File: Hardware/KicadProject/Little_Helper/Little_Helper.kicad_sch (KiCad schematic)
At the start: 1 part, among them U1 ESP32-S3-MINI-1

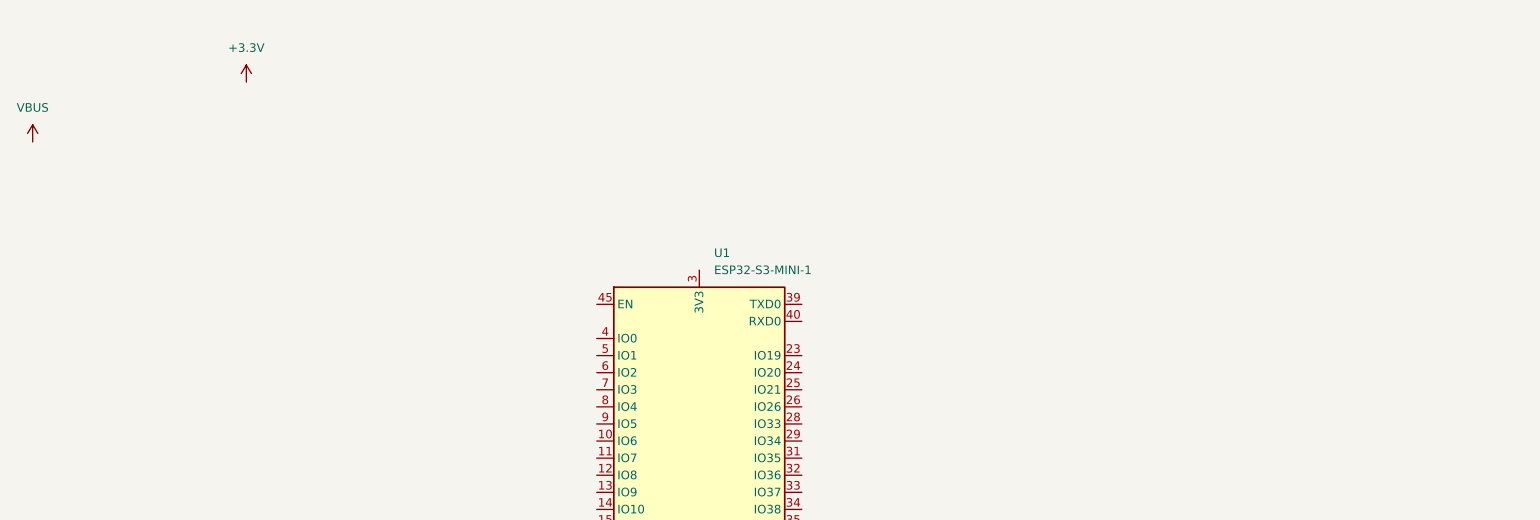
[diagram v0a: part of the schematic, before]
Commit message: fix some library mismatch
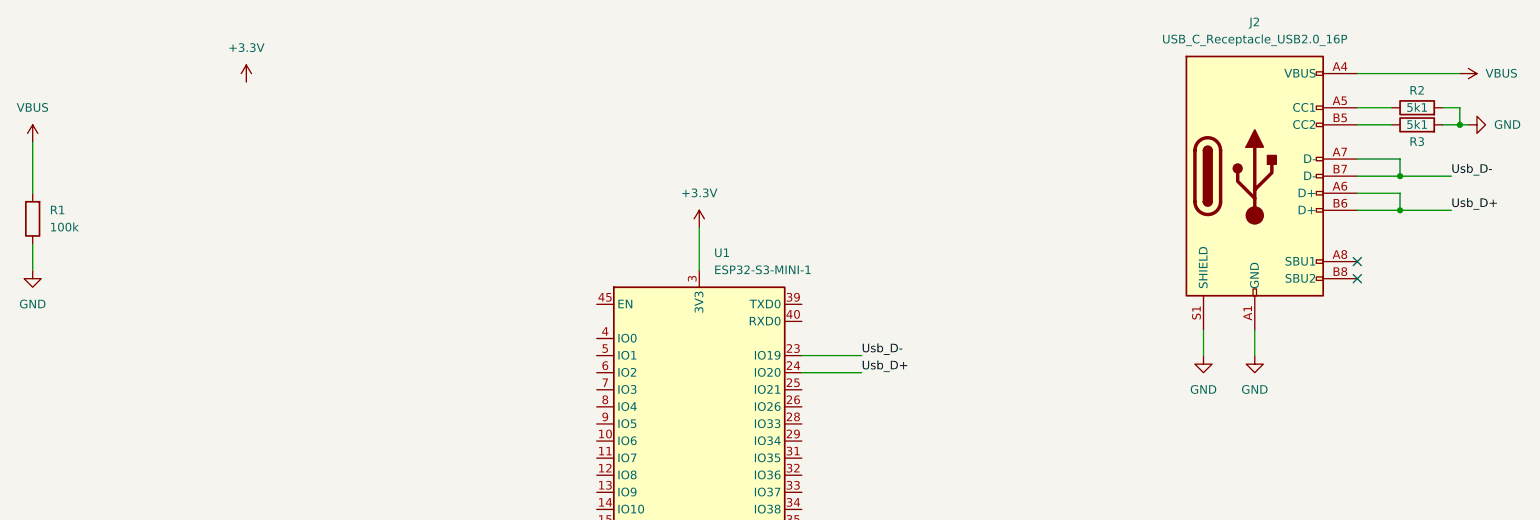
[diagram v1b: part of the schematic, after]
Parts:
- added J2: USB_C_Receptacle_USB2.0_16P, Connector_USB:USB_C_Receptacle_G-Switch_GT-USB-7010ASV, symbol Connector:USB_C_Receptacle_USB2.0_16P
- added R1: 100k, Resistor_SMD:R_0805_2012Metric, symbol Device:R
- added R2, R3: 5k1, Resistor_SMD:R_0805_2012Metric, symbol Device:R
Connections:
- net +3.3V: now also U1.3 (3V3)
- net GND: now also J2.A1 (GND), J2.A12 (GND), J2.B1 (GND), J2.B12 (GND), J2.S1 (SHIELD), R1.1, R2.2, R3.2
- net VBUS: now also J2.A4 (VBUS), J2.A9 (VBUS), J2.B4 (VBUS), J2.B9 (VBUS), R1.2
- net Usb_D-: now reaches U1.23 (IO19)
- net Usb_D-: now also J2.A7 (D-), J2.B7 (D-)
- net Usb_D+: now reaches U1.24 (IO20)
- net Usb_D+: now also J2.A6 (D+), J2.B6 (D+)
- new net: J2.A5 (CC1), R2.1
- new net: J2.B5 (CC2), R3.1
- no-connect marks 0 -> 2

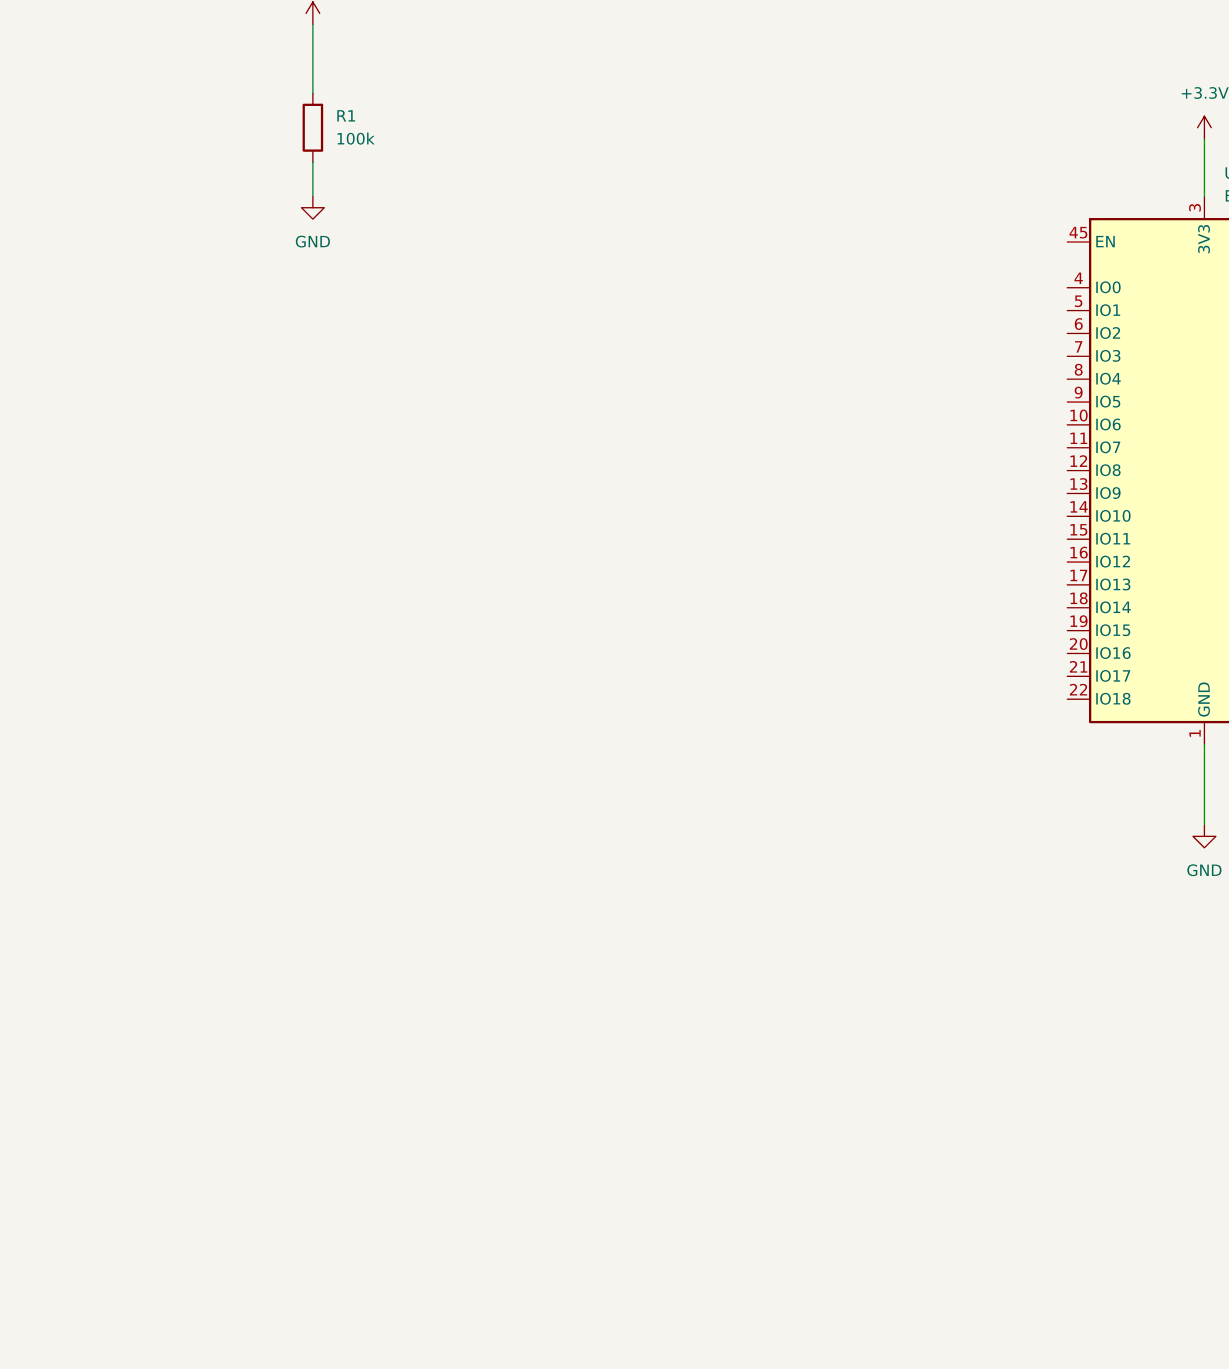
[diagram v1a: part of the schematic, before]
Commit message: add tactile buttons
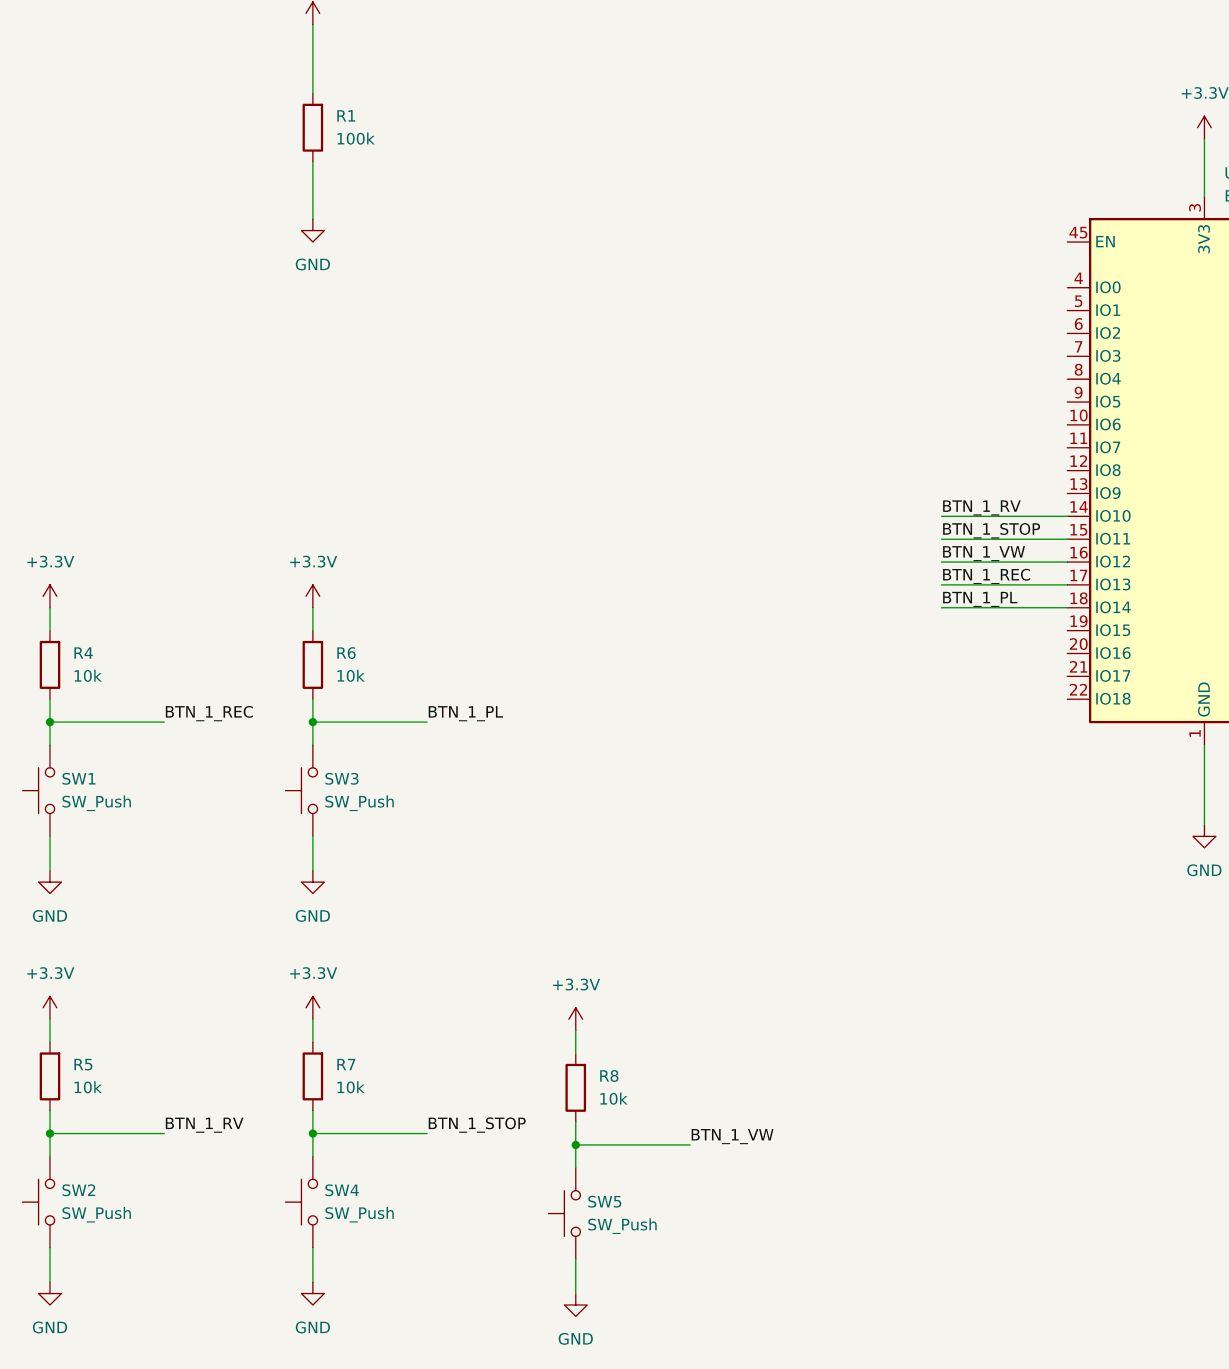
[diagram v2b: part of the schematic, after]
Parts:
- added R4, R5, R6, R7, R8: 10k, Resistor_SMD:R_0805_2012Metric, symbol Device:R
- added SW1, SW2, SW3, SW4, SW5: SW_Push, Button_Switch_THT:SW_PUSH_6mm_H5mm, symbol Switch:SW_Push
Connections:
- net +3.3V: now also R4.2, R5.2, R6.2, R7.2, R8.2
- net GND: now also SW1.1, SW2.1, SW3.1, SW4.1, SW5.1
- net BTN_1_RV: now reaches U1.14 (IO10)
- net BTN_1_RV: now also R5.1, SW2.2
- net BTN_1_STOP: now reaches U1.15 (IO11)
- net BTN_1_STOP: now also R7.1, SW4.2
- net BTN_1_VW: now reaches U1.16 (IO12)
- net BTN_1_VW: now also R8.1, SW5.2
- net BTN_1_REC: now reaches U1.17 (IO13)
- net BTN_1_REC: now also R4.1, SW1.2
- net BTN_1_PL: now reaches U1.18 (IO14)
- net BTN_1_PL: now also R6.1, SW3.2

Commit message: board in progress
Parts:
- removed J2: USB_C_Receptacle_USB2.0_16P, Connector_USB:USB_C_Receptacle_G-Switch_GT-USB-7010ASV, symbol Connector:USB_C_Receptacle_USB2.0_16P
- removed R2, R3: 5k1, Resistor_SMD:R_0805_2012Metric, symbol Device:R
- added C1, C2, C3, C4, C5, C6, C8: 10uF, Capacitor_SMD:C_0603_1608Metric, symbol PCM_Capacitor_AKL:C_0603
- added C7, C9: 1uF, Capacitor_SMD:C_0603_1608Metric, symbol PCM_Capacitor_AKL:C_0603
- added D1: MBR0540, Diode_SMD:D_0805_2012Metric, symbol PCM_Diode_Schottky_AKL:MBR0540
- added D2: LED, LED_SMD:LED_0603_1608Metric, symbol Device:LED
- added D3: WS2812B, LED_SMD:LED_WS2812B_PLCC4_5.0x5.0mm_P3.2mm, symbol LED:WS2812B
- added D4: BAS16, ba_sot:sot_23, symbol ba_diode:BAS16
- added J1: USB_B_Micro, Connector_USB:USB_Micro-B_Wuerth_629105150521_CircularHoles, symbol Connector:USB_B_Micro
- added J2: Conn_01x02_Pin, Connector_Hirose:Hirose_DF13-02P-1.25DSA_1x02_P1.25mm_Vertical, symbol Connector:Conn_01x02_Pin
- added Q1: DMG3415U, Package_TO_SOT_SMD:SOT-23, symbol PCM_Transistor_MOSFET_AKL:DMG3415U
- added R10, R11: 5k1, Resistor_SMD:R_0805_2012Metric, symbol Device:R
- added R3: R2012_100K, ba_res:r2012, symbol ba_res2012:R2012_100K
- added R9: 10k, Resistor_SMD:R_0805_2012Metric, symbol Device:R
- added SW6: SW_SPST, Button_Switch_SMD:SW_SPDT_CK_JS102011SAQN, symbol Switch:SW_SPST
- added SW7, SW8: SW_Push, Button_Switch_SMD:SW_Push_1P1T_NO_Vertical_Wuerth_434133025816, symbol Switch:SW_Push
- added U1: AP2112K-3.3, Package_TO_SOT_SMD:SOT-23-5, symbol Regulator_Linear:AP2112K-3.3
- added U3: MCP73831-2-OT, Package_TO_SOT_SMD:SOT-23-5, symbol Battery_Management:MCP73831-2-OT
- R1: value 100k -> 5k1
- R4: value 10k -> 100k
- renumbered U1 to U2
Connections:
- net +3.3V: now also R1.1, C1.1, C2.1, C3.1, C5.1, C6.1, C7.1, D4.1 (A), R9.2, U1.5 (VOUT); no longer R4.2
- net BTN_1_PL: now also SW5.2, R9.1; no longer R6.1, SW3.2
- net BTN_1_REC: now also R8.1, SW4.2; no longer R4.1, SW1.2
- net BTN_1_RV: now also SW1.2; no longer SW2.2
- net BTN_1_STOP: now also R6.1, SW2.2; no longer R7.1, SW4.2
- net BTN_1_VW: now also R7.1, SW3.2; no longer R8.1, SW5.2
- net GND: now also C1.2, C2.2, C3.2, C4.2, C5.2, C6.2, C7.2, C8.2, C9.2, D3.3 (VSS), J1.4 (ID), J1.5 (GND), J1.6 (Shield), J2.1 (Pin_1), R11.1, R3.2, SW7.1, SW8.1, U1.2 (GND), U3.2 (V_{SS}); no longer R1.1
- net Usb_D+: now also J1.3 (D+)
- net Usb_D-: now also J1.2 (D-)
- net VBUS: now also D1.2 (A), J1.1 (VBUS), Q1.1 (G), R10.1, R3.1, U3.4 (V_{DD}); no longer R1.2
- net NEOPIX: now reaches U2.28 (IO33)
- net NEOPIX: now also D3.4 (DIN)
- net BOOT0: now reaches U2.4 (IO0)
- net BOOT0: now also SW8.2
- net RESET: now reaches U2.45 (EN)
- net RESET: now also R1.2, C9.1, SW7.2
- new net: J2.2 (Pin_2), SW6.2 (B)
- new net: D2.1 (K), U3.1 (STAT)
- new net: D2.2 (A), R10.2
- new net: R11.2, U3.5 (PROG)
- new net: R4.1, U1.3 (EN)
- new net +BATT: C8.1, Q1.3 (D), SW6.1 (A), U3.3 (V_{BAT})
- new net NEOPIX_VDD: C4.1, D1.1 (K), D3.1 (VDD), D4.3 (K), Q1.2 (S), R4.2, U1.1 (VIN)
- no-connect marks 2 -> 32
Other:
- note added: "Orange"
- title: (none) -> Little_Helper
- moved on the sheet: U2

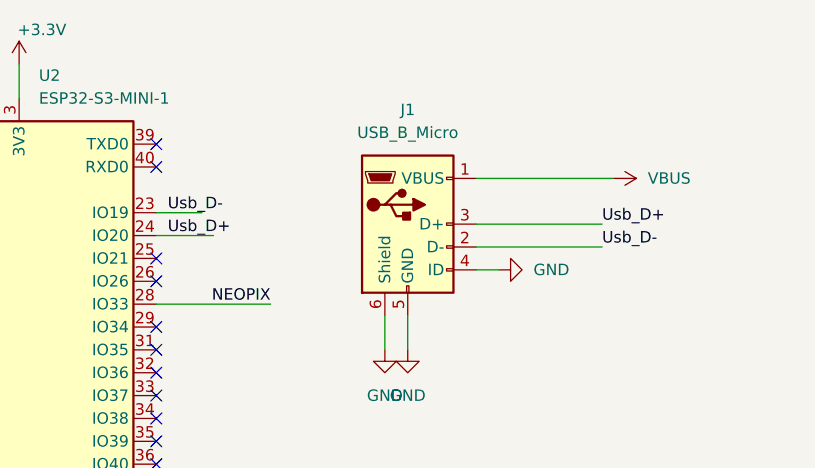
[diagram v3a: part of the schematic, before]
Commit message: change usb micro connector
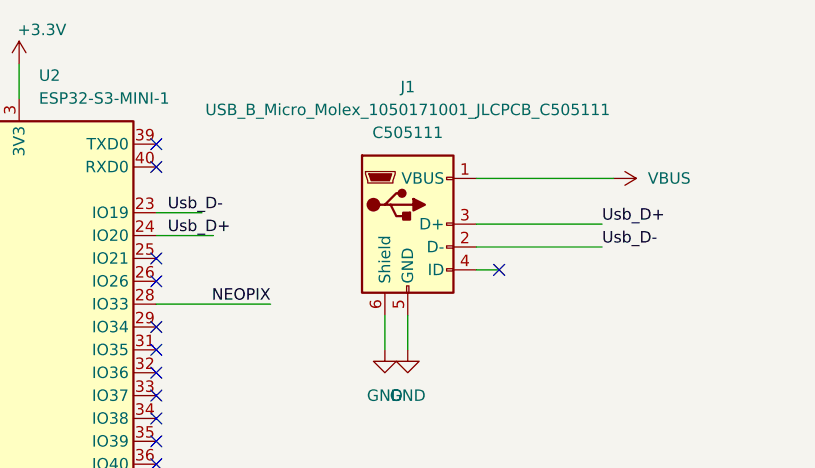
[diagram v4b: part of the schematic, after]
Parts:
- removed J1: USB_B_Micro, Connector_USB:USB_Micro-B_Wuerth_629105150521_CircularHoles, symbol Connector:USB_B_Micro
- added J1: USB_B_Micro_Molex_1050171001_JLCPCB_C505111, Connector_USB:USB_Micro-B_Molex-105017-0001, symbol Connector_USB_WOLKE:USB_B_Micro_Molex_1050171001_JLCPCB_C505111
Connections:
- net GND: now also J1.5 (GND), J1.6 (Shield)
- net Usb_D+: now also J1.3 (D+)
- net Usb_D-: now also J1.2 (D-)
- net VBUS: now also J1.1 (VBUS)
- no-connect marks 32 -> 33
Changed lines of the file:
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@@
 	)
 	(no_connect
+		(at 250.19 40.64)
+	)
+	(no_connect
 		(at 212.09 54.61)
 	)
@@
 	)
 	(symbol
+		(lib_id "Connector_USB_WOLKE:USB_B_Micro_Molex_1050171001_JLCPCB_C505111")
+		(at 240.03 35.56 0)
+		(unit 1)
+		(exclude_from_sim no)
+		(in_bom yes)
+		(on_board yes)
+		(dnp no)
+		(fields_autoplaced yes)
+		(property "Reference" "J1"
+			(at 240.03 20.32 0)
+			(effects
+				(font
+					(size 1.27 1.27)
+				)
+			)
+		)
+		(property "Value" "USB_B_Micro_Molex_1050171001_JLCPCB_C505111"
+			(at 240.03 22.86 0)
+			(effects
+				(font
+					(size 1.27 1.27)
+				)
+			)
+		)
+		(property "Footprint" "Connector_USB:USB_Micro-B_Molex-105017-0001"
+			(at 243.84 36.83 0)
+			(effects
+				(font
+					(size 1.27 1.27)
+				)
+				(hide yes)
+			)
+		)
+		(property "Datasheet" "https://wmsc.lcsc.com/wmsc/upload/file/pdf/v2/lcsc/2004301811_MOLEX-1050171001_C505111.pdf"
+			(at 243.84 36.83 0)
+			(effects
+				(font
+					(size 1.27 1.27)
+				)
+				(hide yes)
+			)
+		)
+		(property "Description" "USB Micro Type B connector"
+			(at 240.03 35.56 0)
+			(effects
+				(font
+					(size 1.27 1.27)
+				)
+				(hide yes)
+			)
+		)
+		(property "MPN" "1050171001"
+			(at 240.03 35.56 0)
+			(effects
+				(font
+					(size 1.27 1.27)
+				)
+				(hide yes)
+			)
+		)
+		(property "MN" "Molex"
+			(at 240.03 35.56 0)
+			(effects
+				(font
+					(size 1.27 1.27)
+				)
+				(hide yes)
+			)
+		)
+		(property "S3N" "JLCPCB"
+			(at 240.03 35.56 0)
+			(effects
+				(font
+					(size 1.27 1.27)
+				)
+				(hide yes)
+			)
+		)
+		(property "S3PN" "C505111"
+			(at 240.03 35.56 0)
+			(effects
+				(font
+					(size 1.27 1.27)
+				)
+				(hide yes)
+			)
+		)
+		(property "LCSC Part #" "C505111"
+			(at 240.03 25.4 0)
+			(effects
+				(font
+					(size 1.27 1.27)
+				)
+			)
+		)
+		(pin "1"
+		)
+		(pin "3"
+		)
+		(pin "5"
+		)
+		(pin "2"
+		)
+		(pin "6"
+		)
+		(pin "4"
+		)
+		(instances
+			(project ""
+				(path "/be456eed-bb99-4947-8d6f-815aa9683d71"
+					(reference "J1")
+					(unit 1)
+				)
+			)
+		)
+	)
+	(symbol
 		(lib_id "Device:LED")
 		(at 134.62 40.64 0)
@@
 	)
 	(symbol
-		(lib_id "Connector:USB_B_Micro")
-		(at 240.03 35.56 0)
-		(unit 1)
-		(exclude_from_sim no)
-		(in_bom yes)
-		(on_board yes)
-		(dnp no)
-		(fields_autoplaced yes)
-		(property "Reference" "J1"
-			(at 240.03 22.86 0)
-			(effects
-				(font
-					(size 1.27 1.27)
-				)
-			)
-		)
-		(property "Value" "USB_B_Micro"
-			(at 240.03 25.4 0)
-			(effects
-				(font
-					(size 1.27 1.27)
-				)
-			)
-		)
-		(property "Footprint" "Connector_USB:USB_Micro-B_Wuerth_629105150521_CircularHoles"
-			(at 243.84 36.83 0)
-			(effects
-				(font
-					(size 1.27 1.27)
-				)
-				(hide yes)
-			)
-		)
-		(property "Datasheet" "~"
-			(at 243.84 36.83 0)
-			(effects
-				(font
-					(size 1.27 1.27)
-				)
-				(hide yes)
-			)
-		)
-		(property "Description" "USB Micro Type B connector"
-			(at 240.03 35.56 0)
-			(effects
-				(font
-					(size 1.27 1.27)
-				)
-				(hide yes)
-			)
-		)
-		(pin "6"
-		)
-		(pin "2"
-		)
-		(pin "1"
-		)
-		(pin "4"
-		)
-		(pin "3"
-		)
-		(pin "5"
-		)
-		(instances
-			(project "Little_Helper"
-				(path "/be456eed-bb99-4947-8d6f-815aa9683d71"
-					(reference "J1")
-					(unit 1)
-				)
-			)
-		)
-	)
-	(symbol
 		(lib_id "power:+BATT")
 		(at 59.69 88.9 0)
@@
 					(unit 1)
 				)
-			)
-		)
-	)
-	(symbol
-		(lib_id "power:GND")
-		(at 250.19 40.64 90)
-		(unit 1)
-		(exclude_from_sim no)
-		(in_bom yes)
-		(on_board yes)
-		(dnp no)
-		(fields_autoplaced yes)
-		(property "Reference" "#PWR08"
-			(at 256.54 40.64 0)
-			(effects
-				(font
-					(size 1.27 1.27)
-				)
-				(hide yes)
-			)
-		)
-		(property "Value" "GND"
-			(at 254 40.6399 90)
-			(effects
-				(font
-					(size 1.27 1.27)
-				)
-				(justify right)
-			)
-		)
-		(property "Footprint" ""
-			(at 250.19 40.64 0)
-			(effects
-				(font
-					(size 1.27 1.27)
-				)
-				(hide yes)
-			)
-		)
-		(property "Datasheet" ""
-			(at 250.19 40.64 0)
-			(effects
-				(font
-					(size 1.27 1.27)
-				)
-				(hide yes)
-			)
-		)
-		(property "Description" "Power symbol creates a global label with name \"GND\" , ground"
-			(at 250.19 40.64 0)
-			(effects
-				(font
-					(size 1.27 1.27)
-				)
-				(hide yes)
-			)
-		)
-		(pin "1"
-		)
-		(instances
-			(project "Little_Helper"
-				(path "/be456eed-bb99-4947-8d6f-815aa9683d71"
-					(reference "#PWR08")
-					(unit 1)
-				)
